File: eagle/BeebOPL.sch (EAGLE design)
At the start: 35 parts, among them IC1 LM324N, IC2 YM3014B, IC3 74LS00N, IC5 74LS02N, IC6 YM3812, IC7 74LS04N, IC9 74HCT688N, J1 1 MHz Bus, J2 Feed-through, J3 3.5mm Jack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

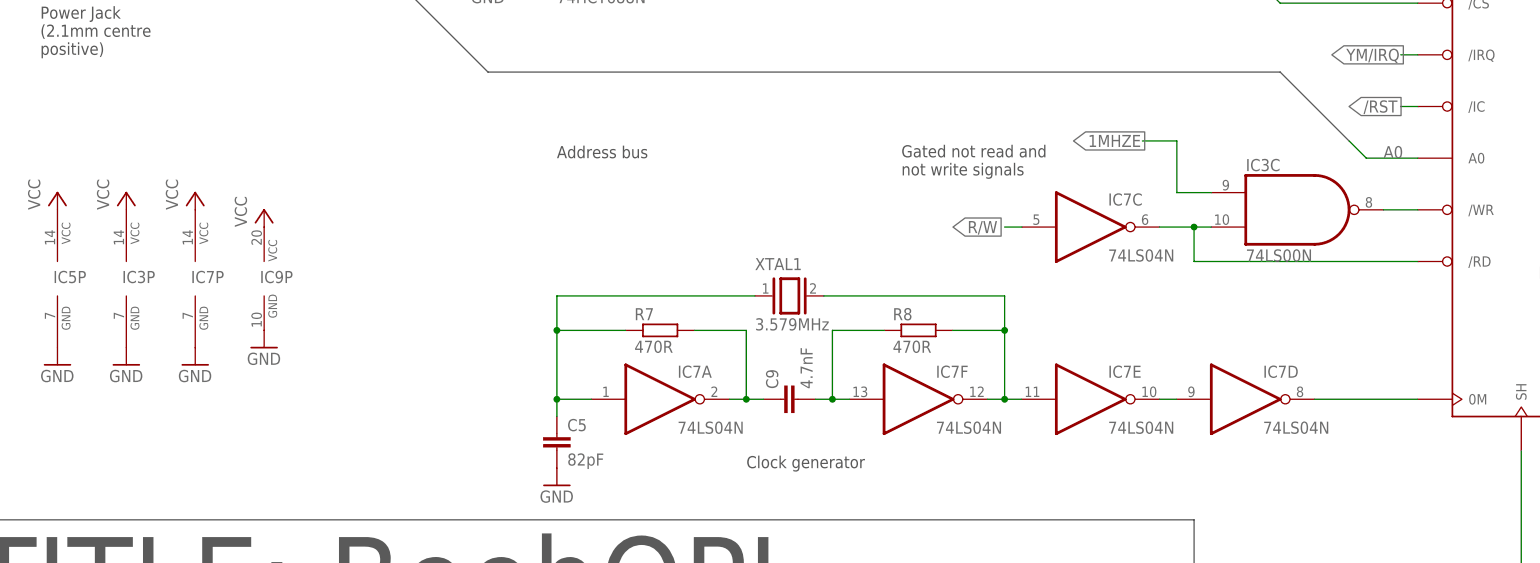
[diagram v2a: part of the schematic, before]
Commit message: Removed 74LS00
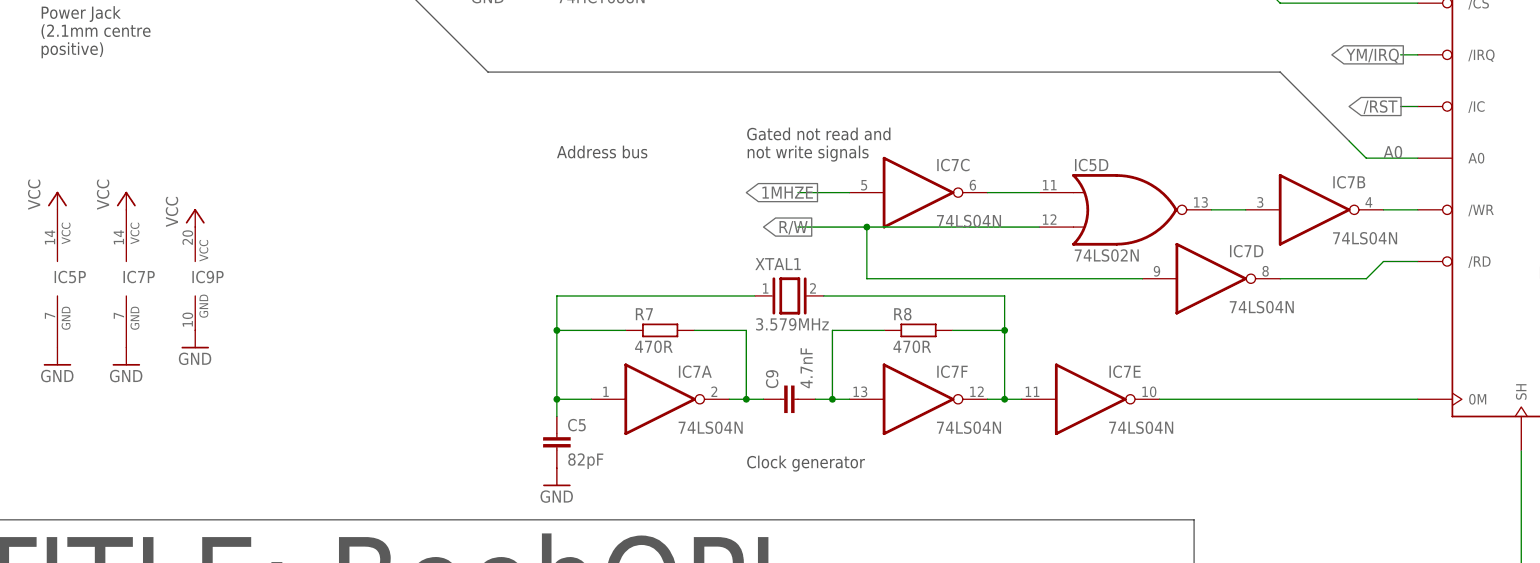
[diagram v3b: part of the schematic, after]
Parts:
- removed IC3: 74LS00N, 74xx-us:74LS00N
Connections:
- removed net /RD: IC3C.I1, IC6./RD, IC7C.O
- removed net N$25: IC6.0M, IC7D.O
- new net N$14: IC6./RD, IC7D.O
- new net N$2: IC5D.O, IC7B.I
- new net N$3: IC5D.I0, IC7C.O
- net 1MHZE: now also IC7C.I; no longer IC3C.I0
- net GND: no longer IC3P.GND
- net N$24: now also IC7B.O; no longer IC3C.O
- net N$26: now also IC6.0M; no longer IC7D.I
- net R/W: now also IC5D.I1, IC7D.I; no longer IC7C.I
- net VCC: no longer IC3P.VCC
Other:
- moved on the sheet: IC7C, IC7D, IC7P, IC9P
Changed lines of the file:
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@@
 <part name="C7" library="resistor" deviceset="C-EU" device="050-024X044" value="10nF"/>
 <part name="C6" library="resistor" deviceset="CPOL-EU" device="E2-5" value="10uF 16V"/>
-<part name="IC3" library="74xx-us" deviceset="74*00" device="N" technology="LS"/>
-<part name="P+2" library="supply1" deviceset="VCC" device=""/>
-<part name="GND3" library="supply1" deviceset="GND" device=""/>
 <part name="IC7" library="74xx-us" deviceset="74*04" device="N" technology="LS"/>
 <part name="P+5" library="supply1" deviceset="VCC" device=""/>
@@
 <text x="-101.6" y="119.38" size="1.778" layer="97">Gated clean not
 page select signal</text>
-<text x="-48.26" y="22.86" size="1.778" layer="97">Gated not read and
+<text x="-71.12" y="25.4" size="1.778" layer="97">Gated not read and
 not write signals</text>
 <text x="-71.12" y="-20.32" size="1.778" layer="97">Clock generator</text>
@@
 <attribute name="VALUE" x="-143.637" y="53.8226" size="1.778" layer="96"/>
 </instance>
-<instance part="IC3" gate="P" x="-162.56" y="7.62"/>
-<instance part="P+2" gate="VCC" x="-162.56" y="20.32"/>
-<instance part="GND3" gate="1" x="-162.56" y="-5.08"/>
-<instance part="IC3" gate="C" x="10.16" y="17.78"/>
 <instance part="IC7" gate="A" x="-83.82" y="-10.16"/>
-<instance part="IC7" gate="P" x="-152.4" y="7.62"/>
-<instance part="P+5" gate="VCC" x="-152.4" y="20.32"/>
-<instance part="GND11" gate="1" x="-152.4" y="-5.08"/>
+<instance part="IC7" gate="P" x="-162.56" y="7.62"/>
+<instance part="P+5" gate="VCC" x="-162.56" y="20.32"/>
+<instance part="GND11" gate="1" x="-162.56" y="-5.08"/>
 <instance part="IC7" gate="F" x="-45.72" y="-10.16"/>
-<instance part="IC7" gate="D" x="2.54" y="-10.16"/>
 <instance part="IC7" gate="E" x="-20.32" y="-10.16"/>
-<instance part="IC7" gate="C" x="-20.32" y="15.24"/>
 <instance part="IC9" gate="A" x="-91.44" y="76.2"/>
 <instance part="P+9" gate="VCC" x="-116.84" y="73.66"/>
 <instance part="GND15" gate="1" x="-109.22" y="50.8"/>
-<instance part="IC9" gate="P" x="-142.24" y="7.62"/>
-<instance part="P+10" gate="VCC" x="-142.24" y="17.78"/>
-<instance part="GND16" gate="1" x="-142.24" y="-2.54"/>
+<instance part="IC9" gate="P" x="-152.4" y="7.62"/>
+<instance part="P+10" gate="VCC" x="-152.4" y="17.78"/>
+<instance part="GND16" gate="1" x="-152.4" y="-2.54"/>
 <instance part="H1" gate="G$1" x="134.62" y="127"/>
 <instance part="H2" gate="G$1" x="134.62" y="116.84"/>
 <instance part="H3" gate="G$1" x="134.62" y="106.68"/>
 <instance part="H4" gate="G$1" x="134.62" y="96.52"/>
+<instance part="IC5" gate="D" x="-15.24" y="17.78"/>
+<instance part="IC7" gate="B" x="12.7" y="17.78"/>
+<instance part="IC7" gate="C" x="-45.72" y="20.32"/>
+<instance part="IC7" gate="D" x="-2.54" y="7.62"/>
 </instances>
 <busses>
@@
 <pinref part="GND4" gate="1" pin="GND"/>
 <wire x1="76.2" y1="-71.12" x2="76.2" y2="-73.66" width="0.1524" layer="91"/>
-</segment>
-<segment>
-<pinref part="IC3" gate="P" pin="GND"/>
-<pinref part="GND3" gate="1" pin="GND"/>
 </segment>
 <segment>
@@
 </segment>
 <segment>
-<pinref part="IC3" gate="P" pin="VCC"/>
-<pinref part="P+2" gate="VCC" pin="VCC"/>
-</segment>
-<segment>
 <pinref part="IC7" gate="P" pin="VCC"/>
 <pinref part="P+5" gate="VCC" pin="VCC"/>
@@
 </segment>
 <segment>
-<wire x1="-2.54" y1="20.32" x2="-7.62" y2="20.32" width="0.1524" layer="91"/>
-<wire x1="-7.62" y1="20.32" x2="-7.62" y2="27.94" width="0.1524" layer="91"/>
-<wire x1="-7.62" y1="27.94" x2="-12.7" y2="27.94" width="0.1524" layer="91"/>
-<label x="-22.86" y="27.94" size="1.778" layer="95" xref="yes"/>
-<pinref part="IC3" gate="C" pin="I0"/>
+<pinref part="IC7" gate="C" pin="I"/>
+<wire x1="-55.88" y1="20.32" x2="-63.5" y2="20.32" width="0.1524" layer="91"/>
+<label x="-71.12" y="20.32" size="1.778" layer="95" xref="yes"/>
 </segment>
 </net>
@@
 </segment>
 <segment>
-<wire x1="-30.48" y1="15.24" x2="-33.02" y2="15.24" width="0.1524" layer="91"/>
-<label x="-40.64" y="15.24" size="1.778" layer="95" xref="yes"/>
-<pinref part="IC7" gate="C" pin="I"/>
+<pinref part="IC5" gate="D" pin="I1"/>
+<wire x1="-27.94" y1="15.24" x2="-53.34" y2="15.24" width="0.1524" layer="91"/>
+<label x="-68.58" y="15.24" size="1.778" layer="95" xref="yes"/>
+<wire x1="-53.34" y1="15.24" x2="-63.5" y2="15.24" width="0.1524" layer="91"/>
+<wire x1="-53.34" y1="15.24" x2="-53.34" y2="7.62" width="0.1524" layer="91"/>
+<junction x="-53.34" y="15.24"/>
+<wire x1="-53.34" y1="7.62" x2="-12.7" y2="7.62" width="0.1524" layer="91"/>
+<pinref part="IC7" gate="D" pin="I"/>
 </segment>
 </net>
@@
 </segment>
 </net>
-<net name="/RD" class="0">
-<segment>
-<wire x1="-10.16" y1="15.24" x2="-5.08" y2="15.24" width="0.1524" layer="91"/>
-<wire x1="-5.08" y1="15.24" x2="-2.54" y2="15.24" width="0.1524" layer="91"/>
-<wire x1="-5.08" y1="15.24" x2="-5.08" y2="10.16" width="0.1524" layer="91"/>
-<junction x="-5.08" y="15.24"/>
-<pinref part="IC6" gate="G$1" pin="/RD"/>
-<wire x1="27.94" y1="10.16" x2="-5.08" y2="10.16" width="0.1524" layer="91"/>
-<pinref part="IC3" gate="C" pin="I1"/>
-<pinref part="IC7" gate="C" pin="O"/>
-</segment>
-</net>
 <net name="N$30" class="0">
 <segment>
@@
 <net name="N$24" class="0">
 <segment>
-<pinref part="IC3" gate="C" pin="O"/>
 <pinref part="IC6" gate="G$1" pin="/WR"/>
 <wire x1="22.86" y1="17.78" x2="27.94" y2="17.78" width="0.1524" layer="91"/>
+<pinref part="IC7" gate="B" pin="O"/>
 </segment>
 </net>
 <net name="N$26" class="0">
 <segment>
-<pinref part="IC7" gate="D" pin="I"/>
-<wire x1="-7.62" y1="-10.16" x2="-10.16" y2="-10.16" width="0.1524" layer="91"/>
 <pinref part="IC7" gate="E" pin="O"/>
-</segment>
-</net>
-<net name="N$25" class="0">
+<pinref part="IC6" gate="G$1" pin="0M"/>
+<wire x1="-10.16" y1="-10.16" x2="27.94" y2="-10.16" width="0.1524" layer="91"/>
+</segment>
+</net>
+<net name="N$2" class="0">
+<segment>
+<pinref part="IC5" gate="D" pin="O"/>
+<pinref part="IC7" gate="B" pin="I"/>
+<wire x1="-2.54" y1="17.78" x2="2.54" y2="17.78" width="0.1524" layer="91"/>
+</segment>
+</net>
+<net name="N$3" class="0">
+<segment>
+<pinref part="IC7" gate="C" pin="O"/>
+<pinref part="IC5" gate="D" pin="I0"/>
+<wire x1="-35.56" y1="20.32" x2="-27.94" y2="20.32" width="0.1524" layer="91"/>
+</segment>
+</net>
+<net name="N$14" class="0">
 <segment>
 <pinref part="IC7" gate="D" pin="O"/>
-<pinref part="IC6" gate="G$1" pin="0M"/>
-<wire x1="12.7" y1="-10.16" x2="27.94" y2="-10.16" width="0.1524" layer="91"/>
-</segment>
-</net>
+<wire x1="7.62" y1="7.62" x2="20.32" y2="7.62" width="0.1524" layer="91"/>
+<wire x1="20.32" y1="7.62" x2="22.86" y2="10.16" width="0.1524" layer="91"/>
+<pinref part="IC6" gate="G$1" pin="/RD"/>
+<wire x1="22.86" y1="10.16" x2="27.94" y2="10.16" width="0.1524" layer="91"/>
+</segment>
+</net>

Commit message: Added resistor networks
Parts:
- added RN1, RN2, RN3, RN4: 2K2, resistor-sil:G08R
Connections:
- net A0: now also RN3.2, RN4.2
- net A1: now also RN3.3, RN4.3
- net A2: now also RN3.4, RN4.4
- net A3: now also RN3.5, RN4.5
- net A4: now also RN3.6, RN4.6
- net A5: now also RN3.7, RN4.7
- net A6: now also RN3.8, RN4.8
- net A7: now also RN3.9, RN4.9
- net D0: now also RN1.2, RN2.2
- net D1: now also RN1.3, RN2.3
- net D2: now also RN1.4, RN2.4
- net D3: now also RN1.5, RN2.5
- net D4: now also RN1.6, RN2.6
- net D5: now also RN1.7, RN2.7
- net D6: now also RN1.8, RN2.8
- net D7: now also RN1.9, RN2.9
- net GND: now also RN2.1, RN4.1
- net VCC: now also RN1.1, RN3.1
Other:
- note added: "DATE: 27 Sept 2016"
- note added: "Designed by: Robert Lazarus (with assistance from David Banks & Mark) Based on the Commodore Sound Expander (Richard Watts & Music Sales Limited, 1985)"
- note added: "REVISION: 0.90"
- note removed: "&04=%00000100 &05=%00000101"
- note removed: "DATE: 11 July 2016"
- note removed: "Designed by: Robert Lazarus (with assistance from David Banks) Based on the Commodore Sound Expander (Richard Watts & Music Sales Limited, 1985)"
- note removed: "REVISION: 0.61"
- moved on the sheet: C5, C6, C7, C9, IC5A, IC5B, IC5C, IC5P, IC7A, IC7D, IC7E, IC7F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
